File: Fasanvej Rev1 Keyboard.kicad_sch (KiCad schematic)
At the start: 141 parts

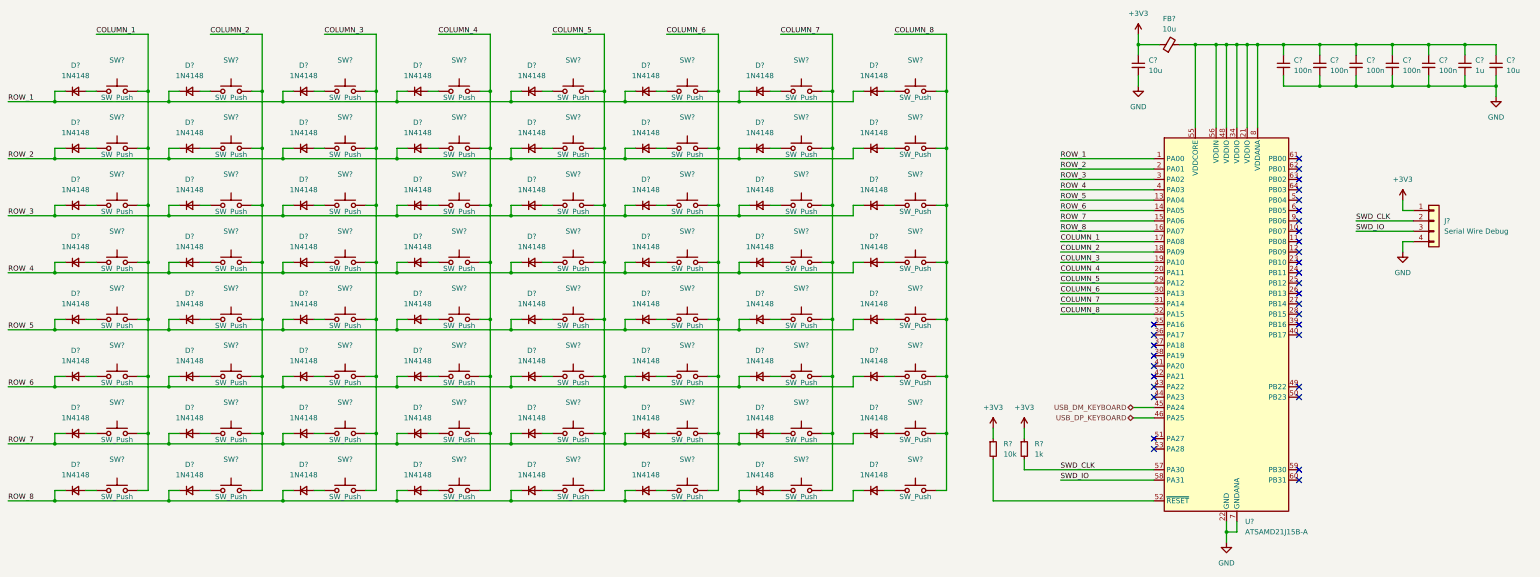
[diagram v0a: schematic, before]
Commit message: Finalized schematics some more. Still missing a few footprints.
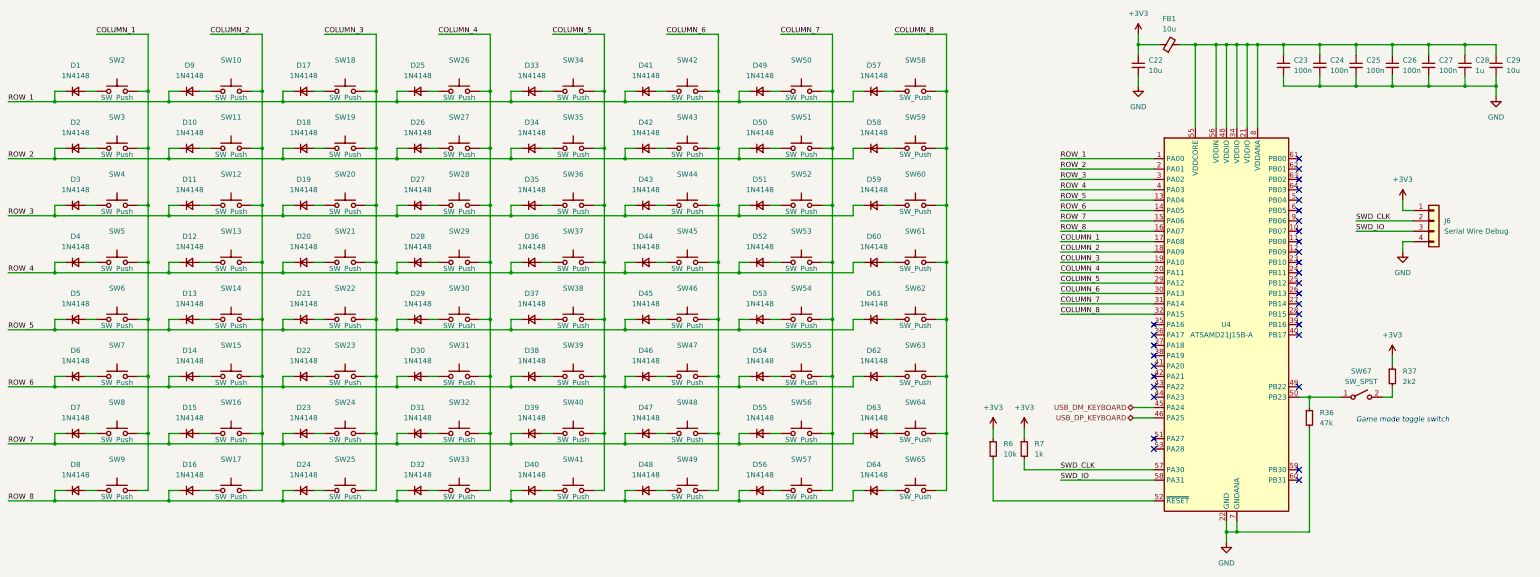
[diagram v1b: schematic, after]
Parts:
- removed SW? (x63): SW_Push, symbol Switch:SW_Push
- added R36: 47k, Resistor_SMD:R_0603_1608Metric_Pad0.98x0.95mm_HandSolder, symbol Device:R_Small
- added R37: 2k2, Resistor_SMD:R_0603_1608Metric_Pad0.98x0.95mm_HandSolder, symbol Device:R_Small
- added SW10, SW11, SW12, SW13, SW14, SW15, SW16, SW17, SW18, SW19, SW2, SW20, SW21, SW22, SW23, SW24, SW25, SW26, SW27, SW28, SW29, SW3, SW30, SW31, SW32, SW33, SW34, SW35, SW36, SW37, SW38, SW39, SW4, SW40, SW41, SW42, SW43, SW44, SW45, SW46, SW47, SW48, SW49, SW5, SW50, SW51, SW52, SW53, SW54, SW55, SW56, SW57, SW59, SW6, SW60, SW61, SW62, SW63, SW64, SW65, SW7, SW8, SW9: SW_Push, Button_Switch_SMD:SW_SPST_TL3342, symbol Switch:SW_Push
- added SW67: SW_SPST, Button_Switch_THT:SW_CuK_JS202011AQN_DPDT_Angled, symbol Switch:SW_SPST
- FB1: renamed from FB?; footprint Capacitor_SMD:C_1206_3216Metric_Pad1.33x1.80mm_HandSolder -> Inductor_SMD:L_1206_3216Metric_Pad1.22x1.90mm_HandSolder
- gave numbers to parts that had none: 77
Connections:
- net +3V3: now also R37.1
- net COLUMN_1: now also SW2.2, SW3.2, SW4.2, SW5.2, SW6.2, SW7.2, SW8.2, SW9.2
- net COLUMN_2: now also SW10.2, SW11.2, SW12.2, SW13.2, SW14.2, SW15.2, SW16.2, SW17.2
- net COLUMN_3: now also SW18.2, SW19.2, SW20.2, SW21.2, SW22.2, SW23.2, SW24.2, SW25.2
- net COLUMN_4: now also SW26.2, SW27.2, SW28.2, SW29.2, SW30.2, SW31.2, SW32.2, SW33.2
- net COLUMN_5: now also SW34.2, SW35.2, SW36.2, SW37.2, SW38.2, SW39.2, SW40.2, SW41.2
- net COLUMN_6: now also SW42.2, SW43.2, SW44.2, SW45.2, SW46.2, SW47.2, SW48.2, SW49.2
- net COLUMN_7: now also SW50.2, SW51.2, SW52.2, SW53.2, SW54.2, SW55.2, SW56.2, SW57.2
- net COLUMN_8: now also SW59.2, SW60.2, SW61.2, SW62.2, SW63.2, SW64.2, SW65.2
- net GND: now also R36.2
- net at D51.2 (A): now also SW52.1
- net at D13.2 (A): now also SW14.1
- net at D6.2 (A): now also SW7.1
- net at D35.2 (A): now also SW36.1
- net at D41.2 (A): now also SW42.1
- net at D49.2 (A): now also SW50.1
- net at D44.2 (A): now also SW45.1
- net at D36.2 (A): now also SW37.1
- net at D4.2 (A): now also SW5.1
- net at D42.2 (A): now also SW43.1
- net at D43.2 (A): now also SW44.1
- net at D23.2 (A): now also SW24.1
- net at D53.2 (A): now also SW54.1
- net at D1.2 (A): now also SW2.1
- net at D40.2 (A): now also SW41.1
- net at D31.2 (A): now also SW32.1
- net at D18.2 (A): now also SW19.1
- net at D8.2 (A): now also SW9.1
- net at D30.2 (A): now also SW31.1
- net at D45.2 (A): now also SW46.1
- net at D60.2 (A): now also SW61.1
- net at D5.2 (A): now also SW6.1
- net at D58.2 (A): now also SW59.1
- net at D20.2 (A): now also SW21.1
- net at D62.2 (A): now also SW63.1
- net at D59.2 (A): now also SW60.1
- net at D52.2 (A): now also SW53.1
- net at D2.2 (A): now also SW3.1
- net at D29.2 (A): now also SW30.1
- net at D16.2 (A): now also SW17.1
- net at D64.2 (A): now also SW65.1
- net at D11.2 (A): now also SW12.1
- net at D56.2 (A): now also SW57.1
- net at D7.2 (A): now also SW8.1
- net at D63.2 (A): now also SW64.1
- net at D34.2 (A): now also SW35.1
- net at D54.2 (A): now also SW55.1
- net at D25.2 (A): now also SW26.1
- net at D38.2 (A): now also SW39.1
- net at D46.2 (A): now also SW47.1
- net at D27.2 (A): now also SW28.1
- net at D12.2 (A): now also SW13.1
- net at D17.2 (A): now also SW18.1
- net at D33.2 (A): now also SW34.1
- net at D39.2 (A): now also SW40.1
- net at D61.2 (A): now also SW62.1
- net at D3.2 (A): now also SW4.1
- net at D32.2 (A): now also SW33.1
- net at D26.2 (A): now also SW27.1
- net at D47.2 (A): now also SW48.1
- net at D19.2 (A): now also SW20.1
- net at D55.2 (A): now also SW56.1
- net at D50.2 (A): now also SW51.1
- net at D48.2 (A): now also SW49.1
- net at D37.2 (A): now also SW38.1
- net at D24.2 (A): now also SW25.1
- net at D22.2 (A): now also SW23.1
- net at D15.2 (A): now also SW16.1
- net at D9.2 (A): now also SW10.1
- net at D28.2 (A): now also SW29.1
- net at D14.2 (A): now also SW15.1
- net at U4.50 (PB23): now also R36.1, SW67.1 (A)
- net at D21.2 (A): now also SW22.1
- net at D10.2 (A): now also SW11.1
- new net: R37.2, SW67.2 (B)
- no-connect marks 32 -> 31
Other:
- note added: "Game mode toggle switch"

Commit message: Made a lot of progress laying out PCB
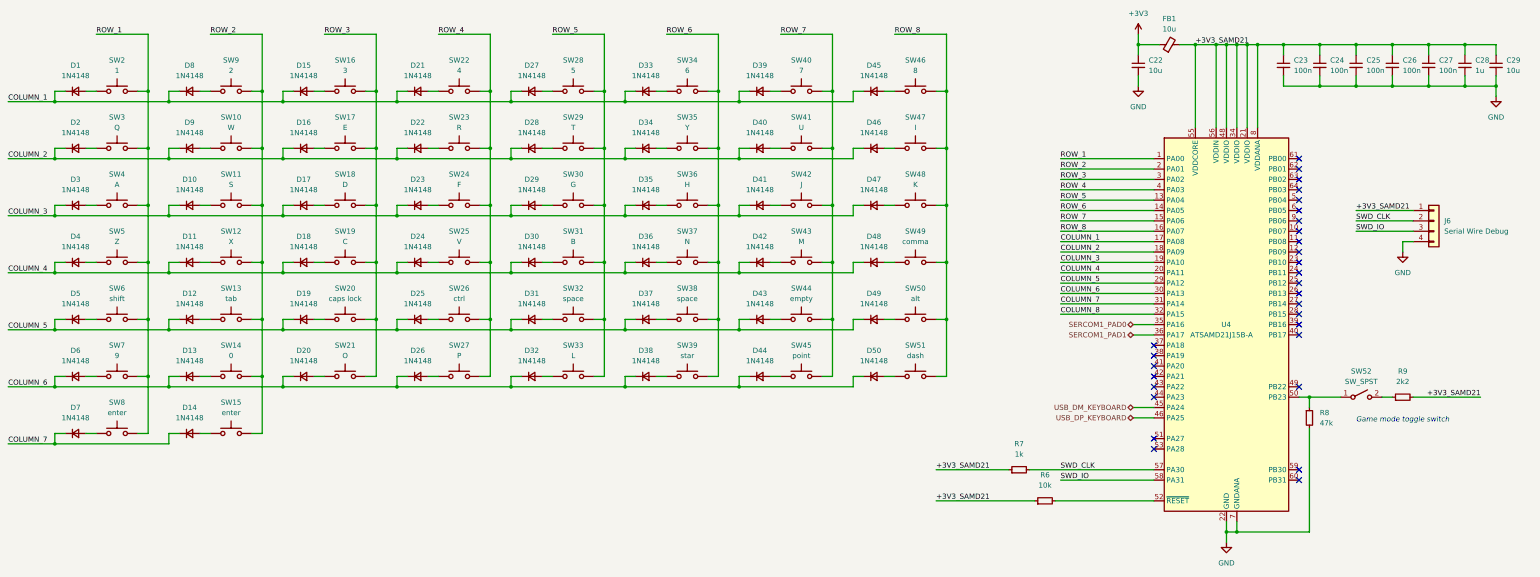
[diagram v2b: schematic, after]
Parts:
- removed D16, D23, D24, D31, D32, D39, D40, D47, D48, D55, D56, D63, D64, D8: 1N4148, Diode_SMD:D_SOD-323_HandSoldering, symbol Device:D_Small
- removed SW17, SW24, SW25, SW32, SW33, SW40, SW41, SW48, SW49, SW56, SW57, SW64, SW65, SW9: SW_Push, Button_Switch_SMD:SW_SPST_TL3342, symbol Switch:SW_Push
- SW10: renamed from SW11; value SW_Push -> W
- SW11: renamed from SW12; value SW_Push -> S
- SW12: renamed from SW13; value SW_Push -> X
- SW13: renamed from SW14; value SW_Push -> tab
- SW14: renamed from SW15; value SW_Push -> 0
- SW15: renamed from SW16; value SW_Push -> enter
- SW16: renamed from SW18; value SW_Push -> 3
- SW17: renamed from SW19; value SW_Push -> E
- SW18: renamed from SW20; value SW_Push -> D
- SW19: renamed from SW21; value SW_Push -> C
- SW2: value SW_Push -> 1
- SW20: renamed from SW22; value SW_Push -> caps lock
- SW21: renamed from SW23; value SW_Push -> O
- SW22: renamed from SW26; value SW_Push -> 4
- SW23: renamed from SW27; value SW_Push -> R
- SW24: renamed from SW28; value SW_Push -> F
- SW25: renamed from SW29; value SW_Push -> V
- SW26: renamed from SW30; value SW_Push -> ctrl
- SW27: renamed from SW31; value SW_Push -> P
- SW28: renamed from SW34; value SW_Push -> 5
- SW29: renamed from SW35; value SW_Push -> T
- SW3: value SW_Push -> Q
- SW30: renamed from SW36; value SW_Push -> G
- SW31: renamed from SW37; value SW_Push -> B
- SW32: renamed from SW38; value SW_Push -> space
- SW33: renamed from SW39; value SW_Push -> L
- SW34: renamed from SW42; value SW_Push -> 6
- SW35: renamed from SW43; value SW_Push -> Y
- SW36: renamed from SW44; value SW_Push -> H
- SW37: renamed from SW45; value SW_Push -> N
- SW38: renamed from SW46; value SW_Push -> space
- SW39: renamed from SW47; value SW_Push -> star
- SW4: value SW_Push -> A
- SW40: renamed from SW50; value SW_Push -> 7
- SW41: renamed from SW51; value SW_Push -> U
- SW42: renamed from SW52; value SW_Push -> J
- SW43: renamed from SW53; value SW_Push -> M
- SW44: renamed from SW54; value SW_Push -> empty
- SW45: renamed from SW55; value SW_Push -> point
- SW46: renamed from SW58; value SW_Push -> 8
- SW47: renamed from SW59; value SW_Push -> I
- SW48: renamed from SW60; value SW_Push -> K
- SW49: renamed from SW61; value SW_Push -> comma
- SW5: value SW_Push -> Z
- SW50: renamed from SW62; value SW_Push -> alt
- SW51: renamed from SW63; value SW_Push -> dash
- SW6: value SW_Push -> shift
- SW7: value SW_Push -> 9
- SW8: value SW_Push -> enter
- SW9: renamed from SW10; value SW_Push -> 2
- renumbered D11 to D10, D12 to D11, D13 to D12, D14 to D13, D15 to D14, D17 to D15, D18 to D16, D19 to D17, D20 to D18, D21 to D19, D22 to D20, D25 to D21, D26 to D22, D27 to D23, D28 to D24, D29 to D25, D30 to D26, D33 to D27, D34 to D28, D35 to D29, D36 to D30, D37 to D31, D38 to D32, D41 to D33, D42 to D34, D43 to D35, D44 to D36, D45 to D37, D46 to D38, D49 to D39, D50 to D40, D51 to D41, D52 to D42, D53 to D43, D54 to D44, D57 to D45, D58 to D46, D59 to D47, D60 to D48, D61 to D49, D62 to D50, D9 to D8, D10 to D9, R36 to R8, R37 to R9, SW67 to SW52
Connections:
- net +3V3: no longer J6.1 (Pin_1), R6.1, R7.1, R9.1
- net COLUMN_1: now also D1.1 (K), D15.1 (K), D21.1 (K), D27.1 (K), D33.1 (K), D39.1 (K), D45.1 (K), D8.1 (K); no longer SW2.2, SW3.2, SW4.2, SW5.2, SW6.2, SW7.2, SW8.2
- net COLUMN_2: now also D16.1 (K), D2.1 (K), D22.1 (K), D28.1 (K), D34.1 (K), D40.1 (K), D46.1 (K), D9.1 (K); no longer SW10.2, SW11.2, SW12.2, SW13.2, SW14.2, SW15.2, SW9.2
- net COLUMN_3: now also D10.1 (K), D17.1 (K), D23.1 (K), D29.1 (K), D3.1 (K), D35.1 (K), D41.1 (K), D47.1 (K); no longer SW16.2, SW17.2, SW18.2, SW19.2, SW20.2, SW21.2
- net COLUMN_4: now also D11.1 (K), D18.1 (K), D24.1 (K), D30.1 (K), D36.1 (K), D4.1 (K), D42.1 (K), D48.1 (K); no longer SW22.2, SW23.2, SW24.2, SW25.2, SW26.2, SW27.2
- net COLUMN_5: now also D12.1 (K), D19.1 (K), D25.1 (K), D31.1 (K), D37.1 (K), D43.1 (K), D49.1 (K), D5.1 (K); no longer SW28.2, SW29.2, SW30.2, SW31.2, SW32.2, SW33.2
- net COLUMN_6: now also D13.1 (K), D20.1 (K), D26.1 (K), D32.1 (K), D38.1 (K), D44.1 (K), D50.1 (K), D6.1 (K); no longer SW34.2, SW35.2, SW36.2, SW37.2, SW38.2, SW39.2
- net COLUMN_7: now also D14.1 (K), D7.1 (K); no longer SW40.2, SW41.2, SW42.2, SW43.2, SW44.2, SW45.2
- net COLUMN_8: no longer SW46.2, SW47.2, SW48.2, SW49.2, SW50.2, SW51.2
- net ROW_1: now also SW2.2, SW3.2, SW4.2, SW5.2, SW6.2, SW7.2, SW8.2; no longer D1.1 (K), D15.1 (K), D21.1 (K), D27.1 (K), D33.1 (K), D39.1 (K), D45.1 (K), D8.1 (K)
- net ROW_2: now also SW10.2, SW11.2, SW12.2, SW13.2, SW14.2, SW15.2, SW9.2; no longer D16.1 (K), D2.1 (K), D22.1 (K), D28.1 (K), D34.1 (K), D40.1 (K), D46.1 (K), D9.1 (K)
- net ROW_3: now also SW16.2, SW17.2, SW18.2, SW19.2, SW20.2, SW21.2; no longer D10.1 (K), D17.1 (K), D23.1 (K), D29.1 (K), D3.1 (K), D35.1 (K), D41.1 (K), D47.1 (K)
- net ROW_4: now also SW22.2, SW23.2, SW24.2, SW25.2, SW26.2, SW27.2; no longer D11.1 (K), D18.1 (K), D24.1 (K), D30.1 (K), D36.1 (K), D4.1 (K), D42.1 (K), D48.1 (K)
- net ROW_5: now also SW28.2, SW29.2, SW30.2, SW31.2, SW32.2, SW33.2; no longer D12.1 (K), D19.1 (K), D25.1 (K), D31.1 (K), D37.1 (K), D43.1 (K), D49.1 (K), D5.1 (K)
- net ROW_6: now also SW34.2, SW35.2, SW36.2, SW37.2, SW38.2, SW39.2; no longer D13.1 (K), D20.1 (K), D26.1 (K), D32.1 (K), D38.1 (K), D44.1 (K), D50.1 (K), D6.1 (K)
- net ROW_7: now also SW40.2, SW41.2, SW42.2, SW43.2, SW44.2, SW45.2; no longer D14.1 (K), D7.1 (K)
- net ROW_8: now also SW46.2, SW47.2, SW48.2, SW49.2, SW50.2, SW51.2
- net at SW52.2 (B): now also R9.1; no longer R9.2
- net +3V3_SAMD21: now reaches C23.1, C24.1, C25.1, C26.1, C27.1, C28.1, C29.1, FB1.2, U4.21 (VDDIO), U4.34 (VDDIO), U4.48 (VDDIO), U4.55 (VDDCORE), U4.56 (VDDIN), U4.8 (VDDANA)
- net +3V3_SAMD21: now also J6.1 (Pin_1), R6.1, R7.1, R9.2
- net SERCOM1_PAD0: now reaches U4.35 (PA16)
- net SERCOM1_PAD1: now reaches U4.36 (PA17)
- no-connect marks 31 -> 29
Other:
- moved on the sheet: R6, R7, R9
